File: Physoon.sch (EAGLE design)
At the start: 38 parts, among them IC2 74AHC1G125DBV, IC3 74AHC1G125DBV, M1 HX1, X1 BU-SMA-V

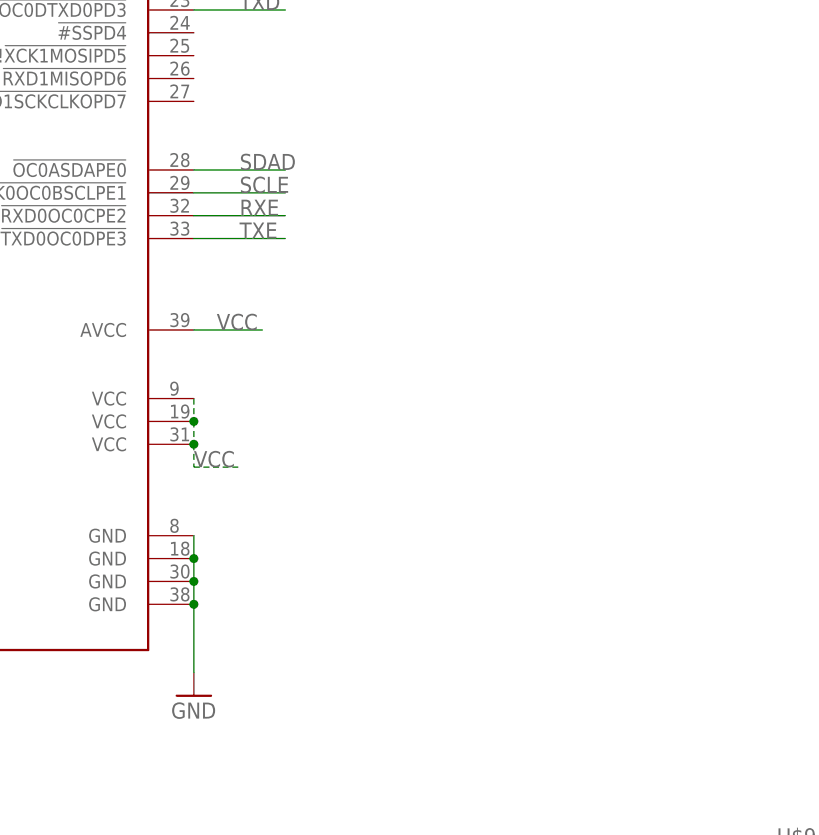
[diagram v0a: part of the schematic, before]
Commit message: Add MCU power filtering, fix drill sizes to Sparkfun DRU
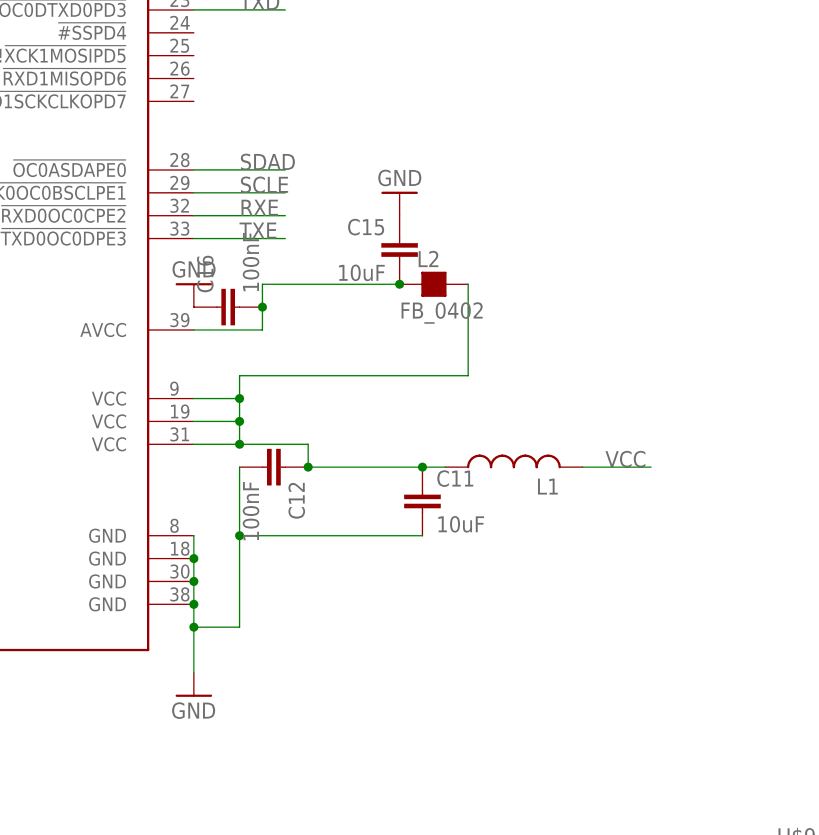
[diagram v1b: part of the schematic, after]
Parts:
- added C11, C15: 10uF, SparkFun:CAP0805
- added C12, C16: 100nF, SparkFun:CAP0805
- added L1: (no value), rcl:L-USL2012C
- added L2: FB_0402, rc-master-smd:FB_0402
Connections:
- new net N$17: C15.2, C16.2, IC1.AVCC, L2.1
- new net N$18: C11.1, C12.1, IC1.VCC@1, IC1.VCC@2, IC1.VCC@3, L1.1, L2.2
- net GND: now also C11.2, C12.2, C15.1, C16.1
- net VCC: now also L1.2; no longer IC1.AVCC, IC1.VCC@1, IC1.VCC@2, IC1.VCC@3
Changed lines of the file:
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@@
 <?xml version="1.0" encoding="utf-8"?>
 <!DOCTYPE eagle SYSTEM "eagle.dtd">
-<eagle version="8.2.0">
+<eagle version="8.2.1">
 <drawing>
 <settings>
@@
 <part name="DIODE" library="Physoon" deviceset="LILYPAD-WEARABLES_LED" device="1206"/>
 <part name="R2" library="SparkFun" deviceset="RESISTOR" device="0805-RES"/>
+<part name="L1" library="rcl" library_urn="urn:adsk.eagle:library:334" deviceset="L-US" device="L2012C"/>
+<part name="C11" library="SparkFun" deviceset="CAP" device="0805" value="10uF"/>
+<part name="L2" library="rc-master-smd" deviceset="FB_" device="0402"/>
+<part name="C15" library="SparkFun" deviceset="CAP" device="0805" value="10uF"/>
+<part name="C16" library="SparkFun" deviceset="CAP" device="0805" value="100nF"/>
+<part name="GND32" library="SparkFun-Aesthetics" deviceset="GND" device=""/>
+<part name="GND33" library="SparkFun-Aesthetics" deviceset="GND" device=""/>
+<part name="C12" library="SparkFun" deviceset="CAP" device="0805" value="100nF"/>
 </parts>
 <sheets>
@@
 <instance part="DIODE" gate="G$1" x="-33.02" y="-25.4" rot="R90"/>
 <instance part="R2" gate="G$1" x="2.54" y="73.66"/>
+<instance part="L1" gate="G$1" x="144.78" y="43.18" rot="R90"/>
+<instance part="C11" gate="G$1" x="134.62" y="38.1"/>
+<instance part="L2" gate="G$1" x="134.62" y="63.5"/>
+<instance part="C15" gate="G$1" x="132.08" y="66.04" rot="MR0"/>
+<instance part="C16" gate="G$1" x="114.3" y="60.96" rot="R90"/>
+<instance part="GND32" gate="1" x="109.22" y="63.5" rot="R180"/>
+<instance part="GND33" gate="1" x="132.08" y="73.66" rot="R180"/>
+<instance part="C12" gate="G$1" x="116.84" y="43.18" rot="R270"/>
 </instances>
 <busses>
@@
 </segment>
 <segment>
-<pinref part="IC1" gate="G$1" pin="VCC@1"/>
-<wire x1="109.22" y1="50.8" x2="109.22" y2="48.26" width="0.1524" layer="91" style="longdash"/>
-<wire x1="109.22" y1="48.26" x2="109.22" y2="45.72" width="0.1524" layer="91" style="longdash"/>
-<wire x1="109.22" y1="45.72" x2="109.22" y2="43.18" width="0.1524" layer="91" style="longdash"/>
-<wire x1="109.22" y1="43.18" x2="114.3" y2="43.18" width="0.1524" layer="91" style="longdash"/>
-<pinref part="IC1" gate="G$1" pin="VCC@2"/>
-<junction x="109.22" y="48.26"/>
-<pinref part="IC1" gate="G$1" pin="VCC@3"/>
-<junction x="109.22" y="45.72"/>
-<label x="109.22" y="43.18" size="1.778" layer="95"/>
-</segment>
-<segment>
 <pinref part="U$10" gate="G$1" pin="OUTPUT"/>
 <wire x1="73.66" y1="185.42" x2="86.36" y2="185.42" width="0.1524" layer="91"/>
@@
 </segment>
 <segment>
-<pinref part="IC1" gate="G$1" pin="AVCC"/>
-<wire x1="109.22" y1="58.42" x2="116.84" y2="58.42" width="0.1524" layer="91"/>
-<label x="111.76" y="58.42" size="1.778" layer="95"/>
-</segment>
-<segment>
 <pinref part="JP4" gate="G$1" pin="4"/>
 <wire x1="60.96" y1="147.32" x2="71.12" y2="147.32" width="0.1524" layer="91"/>
@@
 <wire x1="7.62" y1="73.66" x2="12.7" y2="73.66" width="0.1524" layer="91"/>
 <label x="7.62" y="73.66" size="1.778" layer="95"/>
+</segment>
+<segment>
+<pinref part="L1" gate="G$1" pin="2"/>
+<wire x1="152.4" y1="43.18" x2="160.02" y2="43.18" width="0.1524" layer="91"/>
+<label x="154.94" y="43.18" size="1.778" layer="95"/>
 </segment>
 </net>
@@
 <junction x="109.22" y="30.48"/>
 <pinref part="IC1" gate="G$1" pin="GND@4"/>
-<wire x1="109.22" y1="27.94" x2="109.22" y2="20.32" width="0.1524" layer="91"/>
+<wire x1="109.22" y1="27.94" x2="109.22" y2="25.4" width="0.1524" layer="91"/>
 <junction x="109.22" y="27.94"/>
+<pinref part="C11" gate="G$1" pin="2"/>
+<wire x1="109.22" y1="25.4" x2="109.22" y2="20.32" width="0.1524" layer="91"/>
+<wire x1="134.62" y1="35.56" x2="114.3" y2="35.56" width="0.1524" layer="91"/>
+<wire x1="114.3" y1="35.56" x2="114.3" y2="25.4" width="0.1524" layer="91"/>
+<wire x1="114.3" y1="25.4" x2="109.22" y2="25.4" width="0.1524" layer="91"/>
+<junction x="109.22" y="25.4"/>
+<pinref part="C12" gate="G$1" pin="2"/>
+<wire x1="114.3" y1="43.18" x2="114.3" y2="35.56" width="0.1524" layer="91"/>
+<junction x="114.3" y="35.56"/>
 </segment>
 <segment>
@@
 <wire x1="119.38" y1="132.08" x2="119.38" y2="129.54" width="0.1524" layer="91"/>
 <pinref part="GND16" gate="1" pin="GND"/>
+</segment>
+<segment>
+<pinref part="C16" gate="G$1" pin="1"/>
+<pinref part="GND32" gate="1" pin="GND"/>
+</segment>
+<segment>
+<pinref part="C15" gate="G$1" pin="1"/>
+<pinref part="GND33" gate="1" pin="GND"/>
 </segment>
 </net>
@@
 </segment>
 </net>
+<net name="N$17" class="0">
+<segment>
+<pinref part="L2" gate="G$1" pin="1"/>
+<pinref part="C15" gate="G$1" pin="2"/>
+<wire x1="132.08" y1="63.5" x2="116.84" y2="63.5" width="0.1524" layer="91"/>
+<wire x1="116.84" y1="63.5" x2="116.84" y2="60.96" width="0.1524" layer="91"/>
+<junction x="132.08" y="63.5"/>
+<pinref part="C16" gate="G$1" pin="2"/>
+<wire x1="116.84" y1="60.96" x2="116.84" y2="58.42" width="0.1524" layer="91"/>
+<junction x="116.84" y="60.96"/>
+<pinref part="IC1" gate="G$1" pin="AVCC"/>
+<wire x1="116.84" y1="58.42" x2="109.22" y2="58.42" width="0.1524" layer="91"/>
+</segment>
+</net>
+<net name="N$18" class="0">
+<segment>
+<pinref part="L1" gate="G$1" pin="1"/>
+<wire x1="137.16" y1="43.18" x2="134.62" y2="43.18" width="0.1524" layer="91"/>
+<pinref part="C11" gate="G$1" pin="1"/>
+<junction x="134.62" y="43.18"/>
+<wire x1="134.62" y1="43.18" x2="121.92" y2="43.18" width="0.1524" layer="91"/>
+<pinref part="C12" gate="G$1" pin="1"/>
+<wire x1="121.92" y1="43.18" x2="121.92" y2="45.72" width="0.1524" layer="91"/>
+<junction x="121.92" y="43.18"/>
+<pinref part="IC1" gate="G$1" pin="VCC@3"/>
+<wire x1="121.92" y1="45.72" x2="114.3" y2="45.72" width="0.1524" layer="91"/>
+<pinref part="IC1" gate="G$1" pin="VCC@2"/>
+<wire x1="114.3" y1="45.72" x2="109.22" y2="45.72" width="0.1524" layer="91"/>
+<wire x1="114.3" y1="48.26" x2="109.22" y2="48.26" width="0.1524" layer="91"/>
+<wire x1="114.3" y1="45.72" x2="114.3" y2="48.26" width="0.1524" layer="91"/>
+<junction x="114.3" y="45.72"/>
+<pinref part="IC1" gate="G$1" pin="VCC@1"/>
+<wire x1="109.22" y1="50.8" x2="114.3" y2="50.8" width="0.1524" layer="91"/>
+<wire x1="114.3" y1="48.26" x2="114.3" y2="50.8" width="0.1524" layer="91"/>
+<junction x="114.3" y="48.26"/>
+<wire x1="114.3" y1="50.8" x2="114.3" y2="53.34" width="0.1524" layer="91"/>
+<junction x="114.3" y="50.8"/>
+<pinref part="L2" gate="G$1" pin="2"/>
+<wire x1="114.3" y1="53.34" x2="139.7" y2="53.34" width="0.1524" layer="91"/>
+<wire x1="139.7" y1="53.34" x2="139.7" y2="63.5" width="0.1524" layer="91"/>
+</segment>
+</net>
 </nets>
 </sheet>
@@
 </schematic>
 </drawing>
+<compatibility>
+<note version="8.2" severity="warning">
+Since Version 8.2, Eagle supports online libraries. The ids
+of those online libraries will not be understood (or retained)
+with this version.
+</note>
+</compatibility>
 </eagle>

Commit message: Fix PDI
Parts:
- added R3: 50kOhm, SparkFun:RESISTOR0805-RES
- L1: value (none) -> 10uH
- R2: value (none) -> 50kOhm
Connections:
- net PDI-CLK: now also R3.2
- net VCC: now also R3.1
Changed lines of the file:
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@@
 <part name="GND16" library="SparkFun-Aesthetics" deviceset="GND" device=""/>
 <part name="DIODE" library="Physoon" deviceset="LILYPAD-WEARABLES_LED" device="1206"/>
-<part name="R2" library="SparkFun" deviceset="RESISTOR" device="0805-RES"/>
-<part name="L1" library="rcl" library_urn="urn:adsk.eagle:library:334" deviceset="L-US" device="L2012C"/>
+<part name="R2" library="SparkFun" deviceset="RESISTOR" device="0805-RES" value="50kOhm"/>
+<part name="L1" library="rcl" library_urn="urn:adsk.eagle:library:334" deviceset="L-US" device="L2012C" value="10uH"/>
 <part name="C11" library="SparkFun" deviceset="CAP" device="0805" value="10uF"/>
 <part name="L2" library="rc-master-smd" deviceset="FB_" device="0402"/>
@@
 <part name="GND33" library="SparkFun-Aesthetics" deviceset="GND" device=""/>
 <part name="C12" library="SparkFun" deviceset="CAP" device="0805" value="100nF"/>
+<part name="R3" library="SparkFun" deviceset="RESISTOR" device="0805-RES" value="50kOhm"/>
 </parts>
 <sheets>
@@
 <instance part="GND33" gate="1" x="132.08" y="73.66" rot="R180"/>
 <instance part="C12" gate="G$1" x="116.84" y="43.18" rot="R270"/>
+<instance part="R3" gate="G$1" x="208.28" y="5.08"/>
 </instances>
 <busses>
@@
 <segment>
 <pinref part="U$9" gate="G$1" pin="5"/>
-<wire x1="185.42" y1="-7.62" x2="193.04" y2="-7.62" width="0.1524" layer="91"/>
 <label x="190.5" y="-7.62" size="1.778" layer="95"/>
+<wire x1="185.42" y1="-7.62" x2="215.9" y2="-7.62" width="0.1524" layer="91"/>
+<wire x1="215.9" y1="-7.62" x2="215.9" y2="5.08" width="0.1524" layer="91"/>
+<pinref part="R3" gate="G$1" pin="2"/>
+<wire x1="213.36" y1="5.08" x2="215.9" y2="5.08" width="0.1524" layer="91"/>
 </segment>
 </net>
@@
 <wire x1="175.26" y1="-2.54" x2="165.1" y2="-2.54" width="0.1524" layer="91"/>
 <label x="165.1" y="-5.08" size="1.778" layer="95"/>
+<wire x1="165.1" y1="-2.54" x2="165.1" y2="5.08" width="0.1524" layer="91"/>
+<wire x1="165.1" y1="5.08" x2="203.2" y2="5.08" width="0.1524" layer="91"/>
+<pinref part="R3" gate="G$1" pin="1"/>
 </segment>
 <segment>
